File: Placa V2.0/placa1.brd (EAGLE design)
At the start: 69.5 x 40 mm, 8 parts, among them IC1 LD117AS50TR

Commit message: Super actualización
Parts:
- removed R: 4K7, rcl:R1206
- removed U1: (no value), RHT03_DHT-22_AM2302:RHT03_DHT-22/RA
- added U$1: (no value), DHT11:DHT11
- moved ESP8266 39.2 mm to (19.7, 27.3), turned to 90 degrees
- moved JP1 35.3 mm to (19.1, 18.4), turned to 180 degrees
- moved IC1 25.4 mm to (19.1, 12.1), turned to 0 degrees
- moved C1 25.3 mm to (13.3, 8.89), turned to 0 degrees
- moved OLED 17.3 mm to (15.9, 37.5)
- moved C2 12.1 mm to (24.1, 7.66), turned to 90 degrees
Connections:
- net SCL renamed N$3
- new net N$4: ESP8266.RX, JP1.3
- net 3V3: now also U$1.VCC; no longer R.1, U1.VDD
- net 5V: now also JP1.5
- net DATA: now also U$1.DATA; no longer R.2, U1.DATA
- net GND: now also JP1.1, U$1.GND; no longer U1.GND
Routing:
- net GND: track 0.00 -> 113.9 mm
- net DATA: track 74.2 -> 28.7 mm
- net N$4: track 0.00 -> 9.90 mm
- net 3V3: track 126.5 -> 118.0 mm, vias 1 -> 0
- net N$3: track 33.0 -> 24.7 mm
- net SDA: track 24.1 -> 21.4 mm
- net 5V: track 10.7 -> 12.2 mm
- removed copper zone on layer 16, net GND
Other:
- board size 69.5 x 40 mm -> 35.2 x 55.9 mm

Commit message: cambios en placa
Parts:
- removed U$1: (no value), DHT11:DHT11
- added J1: STEREOJACKSJ1-352XNG, Ai_Connectors:SJ1-352XNG
- added U1: (no value), dht22:RHT03_DHT-22/RA
- moved C2 18.4 mm to (16.5, 24.4), turned to 180 degrees
- moved JP1 14.3 mm to (33.3, 17.5)
- moved IC1 13.8 mm to (32.8, 11.1)
- moved C1 13.0 mm to (20.1, 20.0)
- moved ESP8266 5.64 mm to (25.2, 28.6)
- moved OLED 5.64 mm to (21.4, 38.7)
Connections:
- removed net N$4: ESP8266.RX, JP1.3
- new net RX: ESP8266.RX, J1.RNG, J1.RSH
- net 3V3: now also J1.TIP, J1.TSH, U1.VDD; no longer U$1.VCC
- net DATA: now also U1.DATA; no longer U$1.DATA
- net GND: now also J1.GND, U1.GND; no longer U$1.GND
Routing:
- net RX: track 0.00 -> 29.3 mm
- net GND: track 113.9 -> 138.8 mm
- net 5V: track 12.2 -> 24.8 mm
- net N$4: track 9.90 -> 0.00 mm, vias 0 -> 1
- net 3V3: track 118.0 -> 125.5 mm
- net DATA: track 28.7 -> 30.8 mm
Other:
- board size 35.2 x 55.9 mm -> 45 x 57.6 mm

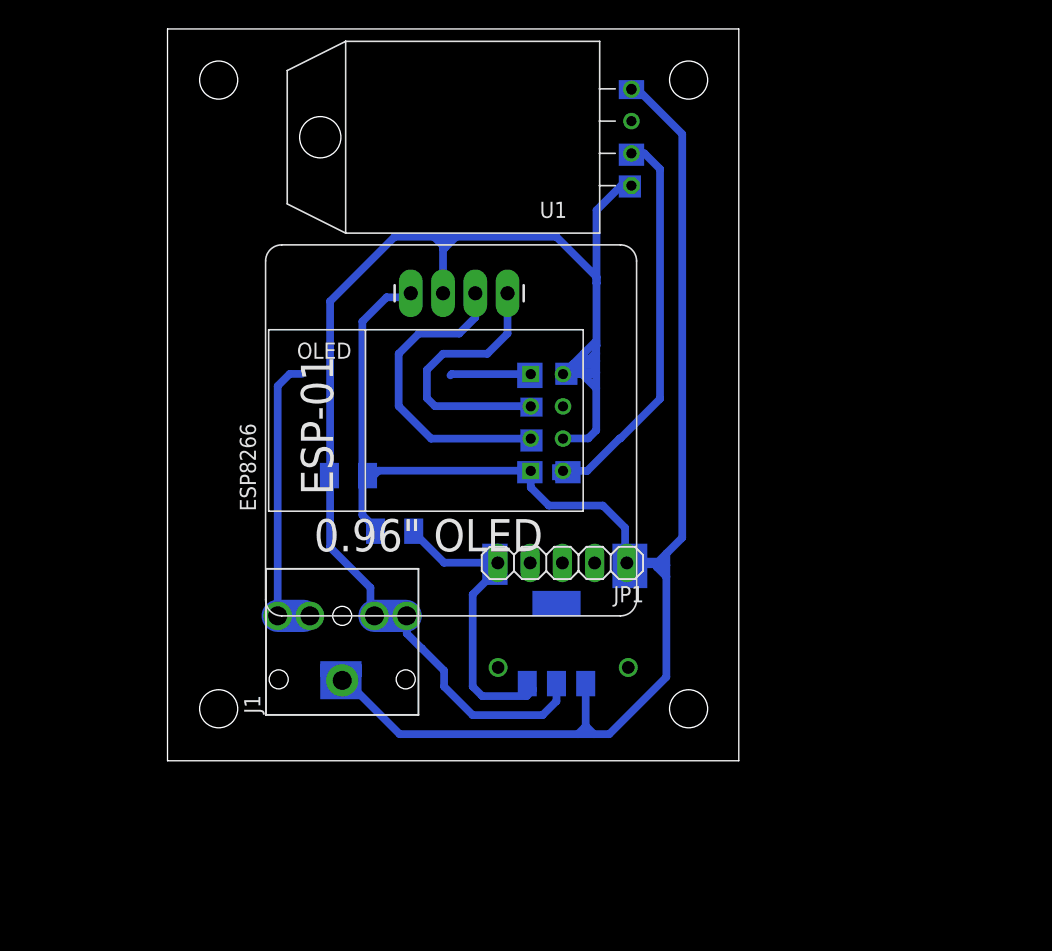
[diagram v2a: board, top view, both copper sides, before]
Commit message: cambios con bug de pantalla
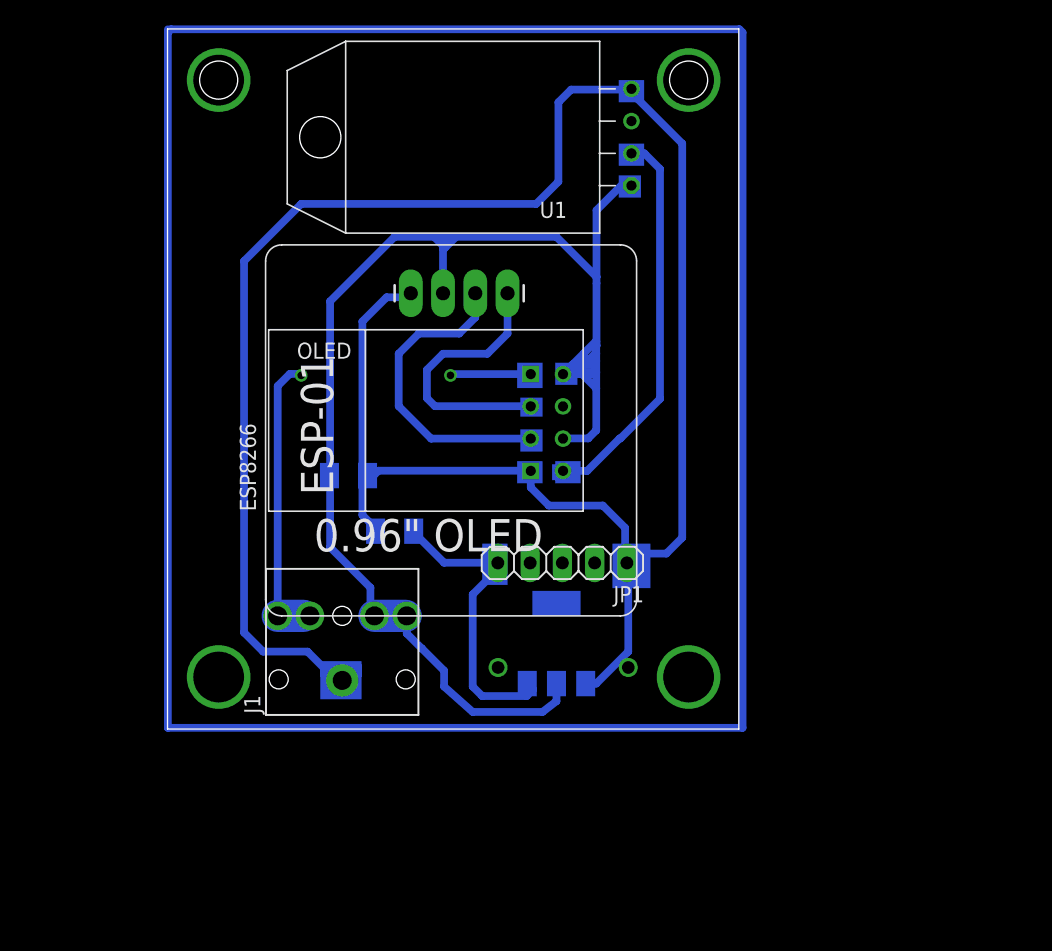
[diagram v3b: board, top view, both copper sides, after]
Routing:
- net N$8: track 0.00 -> 200.5 mm
- net GND: track 138.8 -> 181.0 mm
- net 3V3: track 125.5 -> 124.7 mm
- net RX: vias 0 -> 1
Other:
- board size 45 x 57.6 mm -> 45 x 55.1 mm
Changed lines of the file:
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@@
 <board>
 <plain>
-<wire x1="2.2225" y1="1.905" x2="47.2025" y2="1.905" width="0" layer="20"/>
-<wire x1="47.2025" y1="1.905" x2="47.2025" y2="59.525" width="0" layer="20"/>
+<wire x1="2.2225" y1="4.405" x2="47.2025" y2="4.405" width="0" layer="20"/>
+<wire x1="47.2025" y1="4.405" x2="47.2025" y2="59.525" width="0" layer="20"/>
 <wire x1="47.2025" y1="59.525" x2="2.2225" y2="59.525" width="0" layer="20"/>
-<wire x1="2.2225" y1="59.525" x2="2.2225" y2="1.905" width="0" layer="20"/>
+<wire x1="2.2225" y1="59.525" x2="2.2225" y2="4.405" width="0" layer="20"/>
 <dimension x1="40.75" y1="18.75" x2="40.75" y2="9.25" x3="26.5" y3="14" textsize="1.778" layer="20"/>
 <hole x="43.25" y="55.5" drill="3"/>
 <hole x="6.25" y="55.5" drill="3"/>
-<hole x="6.25" y="6" drill="3"/>
-<hole x="43.25" y="6" drill="3"/>
-<rectangle x1="37.75" y1="54" x2="39.75" y2="55.5" layer="16"/>
 <rectangle x1="37.75" y1="48.75" x2="39.75" y2="50.5" layer="16"/>
 <rectangle x1="37.75" y1="46.25" x2="39.5" y2="47.75" layer="16"/>
@@
 <rectangle x1="14.25" y1="8.5" x2="17.5" y2="9.75" layer="16"/>
 <rectangle x1="27" y1="15.75" x2="29" y2="19" layer="16"/>
-<rectangle x1="37.25" y1="15.5" x2="40" y2="19" layer="16"/>
+<rectangle x1="37.75" y1="53.75" x2="39.5" y2="55.5" layer="16"/>
+<rectangle x1="39.5" y1="53.75" x2="39.75" y2="55.5" layer="16"/>
+<rectangle x1="37.25" y1="15.5" x2="40.25" y2="19" layer="16"/>
+<dimension x1="47.25" y1="59.5" x2="49" y2="4.5" x3="60.5" y3="32" textsize="1.778" layer="20" dtype="vertical"/>
+<dimension x1="47.2025" y1="4.405" x2="2.25" y2="3.75" x3="24.72625" y3="-4.75" textsize="1.778" layer="20" dtype="horizontal"/>
 </plain>
 <attributes>
@@
 <wire x1="14.9725" y1="23.655421875" x2="15.025" y2="23.602921875" width="0.6096" layer="16"/>
 <wire x1="32.8475" y1="7.9825" x2="32.8475" y2="6.5975" width="0.6096" layer="16"/>
-<wire x1="32.8475" y1="6.5975" x2="31.75" y2="5.5" width="0.6096" layer="16"/>
-<wire x1="31.75" y1="5.5" x2="26.25" y2="5.5" width="0.6096" layer="16"/>
-<wire x1="26.25" y1="5.5" x2="24" y2="7.75" width="0.6096" layer="16"/>
+<wire x1="32.8475" y1="6.5975" x2="31.75" y2="5.75" width="0.6096" layer="16"/>
+<wire x1="31.75" y1="5.75" x2="26.25" y2="5.75" width="0.6096" layer="16"/>
+<wire x1="26.25" y1="5.75" x2="24" y2="7.75" width="0.6096" layer="16"/>
 <wire x1="24" y1="7.75" x2="24" y2="9" width="0.6096" layer="16"/>
 <wire x1="24" y1="9" x2="22.25" y2="10.75" width="0.6096" layer="16"/>
@@
 <wire x1="23.915" y1="42.452959375" x2="23.207959375" y2="43.16" width="0.6096" layer="16"/>
 <wire x1="38.75" y1="47.19" x2="37.94" y2="47.19" width="0.6096" layer="16"/>
-<wire x1="36" y1="45.25" x2="36" y2="39.49513125" width="0.6096" layer="16"/>
+<wire x1="36" y1="45.25" x2="36" y2="40" width="0.6096" layer="16"/>
 <wire x1="37.94" y1="47.19" x2="36" y2="45.25" width="0.6096" layer="16"/>
 </signal>
@@
 <contactref element="ESP8266" pad="TX"/>
 <wire x1="35.267425" y1="24.73" x2="33.3625" y2="24.73" width="0.6096" layer="16"/>
-<wire x1="35.267425" y1="24.73" x2="35.965" y2="24.73" width="0" layer="19" extent="1-16"/>
 <contactref element="U1" pad="DATA"/>
 <wire x1="38.75" y1="49.73" x2="39.77" y2="49.73" width="0.6096" layer="16"/>
@@
 <wire x1="17.9725" y1="24.3575" x2="18.4475" y2="24.3575" width="0.6096" layer="16"/>
 <wire x1="18.4475" y1="24.3575" x2="18.835" y2="24.745" width="0.6096" layer="16"/>
-<wire x1="15.9775" y1="8.235" x2="16.265" y2="8.235" width="0.6096" layer="16"/>
-<wire x1="16.265" y1="8.235" x2="20.5" y2="4" width="0.6096" layer="16"/>
-<wire x1="34.532490625" y1="4" x2="20.5" y2="4" width="0.6096" layer="16"/>
-<wire x1="35.796975" y1="4" x2="34.532490625" y2="4" width="0.6096" layer="16"/>
-<wire x1="35.796975" y1="4" x2="37" y2="4" width="0.6096" layer="16"/>
-<wire x1="41.5" y1="8.5" x2="37" y2="4" width="0.6096" layer="16"/>
-<wire x1="35.1475" y1="7.9825" x2="35.1475" y2="4.615009375" width="0.6096" layer="16"/>
-<wire x1="35.1475" y1="4.615009375" x2="34.532490625" y2="4" width="0.6096" layer="16"/>
-<wire x1="35.1475" y1="4.615009375" x2="35.181965625" y2="4.615009375" width="0.6096" layer="16"/>
-<wire x1="35.181965625" y1="4.615009375" x2="35.796975" y2="4" width="0.6096" layer="16"/>
+<wire x1="16.265" y1="8.235" x2="15.9775" y2="8.235" width="0.6096" layer="16"/>
 <contactref element="U1" pad="GND"/>
-<wire x1="41.5" y1="18.220159375" x2="41.5" y2="17.309153125" width="0.6096" layer="16"/>
-<wire x1="41.5" y1="16.39814375" x2="41.5" y2="17.309153125" width="0.6096" layer="16"/>
-<wire x1="41.5" y1="16.39814375" x2="41.5" y2="8.5" width="0.6096" layer="16"/>
 <wire x1="30.8225" y1="24.73" x2="30.8225" y2="23.4275" width="0.6096" layer="16"/>
 <wire x1="30.8225" y1="23.4275" x2="32.25" y2="22" width="0.6096" layer="16"/>
 <wire x1="32.25" y1="22" x2="36.5" y2="22" width="0.6096" layer="16"/>
 <wire x1="36.5" y1="22" x2="38.25" y2="20.25" width="0.6096" layer="16"/>
-<wire x1="38.25" y1="20.25" x2="38.25" y2="17.625" width="0.6096" layer="16"/>
-<wire x1="38.25" y1="17.625" x2="38.3925" y2="17.4825" width="0.6096" layer="16"/>
-<wire x1="38.3925" y1="17.4825" x2="40" y2="17.4825" width="0.6096" layer="16"/>
-<wire x1="40" y1="17.4825" x2="40.75" y2="17.4825" width="0.6096" layer="16"/>
-<wire x1="41.326653125" y1="17.4825" x2="40.762340625" y2="17.4825" width="0.6096" layer="16"/>
-<wire x1="41.326653125" y1="17.4825" x2="41.5" y2="17.309153125" width="0.6096" layer="16"/>
-<wire x1="40.75" y1="17.4825" x2="40.762340625" y2="17.4825" width="0.6096" layer="16"/>
-<wire x1="40.762340625" y1="17.4825" x2="41.5" y2="18.220159375" width="0.6096" layer="16"/>
-<wire x1="40.75" y1="17.4825" x2="40.75" y2="17.14814375" width="0.6096" layer="16"/>
-<wire x1="40.75" y1="17.14814375" x2="41.5" y2="16.39814375" width="0.6096" layer="16"/>
-<wire x1="38.75" y1="54.81" x2="39.19" y2="54.81" width="0.6096" layer="16"/>
-<wire x1="39.19" y1="54.81" x2="42.75" y2="51.25" width="0.6096" layer="16"/>
-<wire x1="42.75" y1="51.25" x2="42.75" y2="19.470159375" width="0.6096" layer="16"/>
+<wire x1="38.25" y1="17.84769375" x2="38.25" y2="20.25" width="0.6096" layer="16"/>
+<wire x1="38.25" y1="17.84769375" x2="38.25" y2="17.625" width="0.6096" layer="16"/>
+<wire x1="38.3925" y1="17.4825" x2="38.25" y2="17.625" width="0.6096" layer="16"/>
 <wire x1="42.75" y1="19.470159375" x2="41.5" y2="18.220159375" width="0.6096" layer="16"/>
-<wire x1="40" y1="17.4825" x2="41.326653125" y2="17.4825" width="0.8128" layer="16"/>
+<wire x1="15.9775" y1="8.235" x2="15.515" y2="8.235" width="0.6096" layer="16"/>
+<wire x1="13.25" y1="10.5" x2="9.75" y2="10.5" width="0.6096" layer="16"/>
+<wire x1="9.75" y1="10.5" x2="8.25" y2="12" width="0.6096" layer="16"/>
+<wire x1="8.25" y1="12" x2="8.25" y2="41.25" width="0.6096" layer="16"/>
+<wire x1="8.25" y1="41.25" x2="12.75" y2="45.75" width="0.6096" layer="16"/>
+<wire x1="12.75" y1="45.75" x2="31.25" y2="45.75" width="0.6096" layer="16"/>
+<wire x1="31.25" y1="45.75" x2="33" y2="47.5" width="0.6096" layer="16"/>
+<wire x1="33" y1="47.5" x2="33" y2="53.75" width="0.6096" layer="16"/>
+<wire x1="33" y1="53.75" x2="34" y2="54.75" width="0.6096" layer="16"/>
+<wire x1="15.515" y1="8.235" x2="13.25" y2="10.5" width="0.6096" layer="16"/>
+<wire x1="38.69" y1="54.75" x2="38.75" y2="54.81" width="0.6096" layer="16"/>
+<wire x1="34" y1="54.75" x2="38.69" y2="54.75" width="0.6096" layer="16"/>
+<wire x1="38.622465625" y1="18.220159375" x2="38.25" y2="17.84769375" width="0.6096" layer="16"/>
+<wire x1="41.5" y1="18.220159375" x2="38.622465625" y2="18.220159375" width="0.6096" layer="16"/>
+<wire x1="38.75" y1="54.81" x2="38.75" y2="54.5" width="0.6096" layer="16"/>
+<wire x1="42.75" y1="50.5" x2="42.75" y2="19.470159375" width="0.6096" layer="16"/>
+<wire x1="38.75" y1="54.5" x2="42.75" y2="50.5" width="0.6096" layer="16"/>
+<wire x1="35.1475" y1="7.9825" x2="35.9825" y2="7.9825" width="0.6096" layer="16"/>
+<wire x1="38.5" y1="10.5" x2="38.5" y2="17.375" width="0.6096" layer="16"/>
+<wire x1="38.5" y1="17.375" x2="38.3925" y2="17.4825" width="0.6096" layer="16"/>
+<wire x1="35.9825" y1="7.9825" x2="38.5" y2="10.5" width="0.6096" layer="16"/>
 </signal>
 <signal name="SDA">
@@
 <wire x1="24.6" y1="32.35" x2="24.5" y2="32.25" width="0.6096" layer="16"/>
 <wire x1="10.8975" y1="13.315" x2="12.9415" y2="13.315" width="2.54" layer="16"/>
+<via x="24.5" y="32.25" extent="1-16" drill="0.6"/>
 <wire x1="12.8025" y1="32.365" x2="24.5" y2="32.25" width="0" layer="19" extent="16-16"/>
 </signal>
@@
 <via x="28.25" y="9.25" extent="1-16" drill="1"/>
 </signal>
-<signal name="N$6">
-<via x="38.75" y="54.75" extent="1-16" drill="0.8" diameter="1.3" shape="octagon"/>
+<signal name="N$8">
+<wire x1="2.25" y1="59.5" x2="2.25" y2="59.25" width="0.6096" layer="16"/>
+<wire x1="2.25" y1="59.25" x2="2.25" y2="4.5" width="0.6096" layer="16"/>
+<wire x1="2.25" y1="4.5" x2="47.5" y2="4.5" width="0.6096" layer="16"/>
+<wire x1="47.5" y1="4.5" x2="47.5" y2="59.25" width="0.6096" layer="16"/>
+<wire x1="47.5" y1="59.25" x2="47.25" y2="59.5" width="0.6096" layer="16"/>
+<wire x1="47.25" y1="59.5" x2="2.5" y2="59.5" width="0.6096" layer="16"/>
+<wire x1="2.5" y1="59.5" x2="2.25" y2="59.25" width="0.6096" layer="16"/>
+</signal>
+<signal name="N$9">
+<via x="6.25" y="55.5" extent="1-16" drill="4"/>
+</signal>
+<signal name="N$10">
+<via x="43.25" y="55.5" extent="1-16" drill="4"/>
+</signal>
+<signal name="N$11">
+<via x="43.25" y="8.5" extent="1-16" drill="4"/>
+</signal>
+<signal name="N$12">
+<via x="6.25" y="8.5" extent="1-16" drill="4"/>
+</signal>
+<signal name="N$13">
+<via x="12.75" y="32.25" extent="1-16" drill="0.6"/>
 </signal>
 </signals>
